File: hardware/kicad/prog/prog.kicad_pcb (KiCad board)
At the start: 4 copper layers, 174 x 134 mm, 123 parts, among them J1 AES_PROG, J2 Câble PROG-CHA, J3 CONF P, J4 CONF V, U1 AMS1117-3.3, U10 iCE40HX4K-TQ144, U11 W9825G6KH-6, U12 iCE40HX4K-TQ144, U13 W9825G6KH-6, U2 AP2112K-1.2, U3 74LVC16244A, U4 74LVC16244A, U5 74LVC16244A, U6 74LVC16245A, U7 74LVC16245A, U8 74AHCT125, U9 74LVC1G07, X1 25 MHz 3,3 V, X2 25 MHz 3,3 V

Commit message: PCB : vias vers les plans écartés de toutes les pastilles CMS
Freerouting refuse un via sur une pastille, même de son réseau.

Co-Authored-By: Claude Opus 5.5 <noreply@anthropic.com>
Claude-Session: https://claude.ai/code/session_01WKfXP1YJ8otGxZ5dsY6Agh
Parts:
- moved R6 39.1 mm to (128.6, 140.3)
- moved R4 34.7 mm to (131.1, 140.3)
- moved R5 28.2 mm to (128.6, 132.3)
- moved R3 25.7 mm to (128.6, 136.3)
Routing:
- net +3V3: track 137.5 -> 134.7 mm, vias 115 -> 114
- net GND: track 245.2 -> 246.8 mm

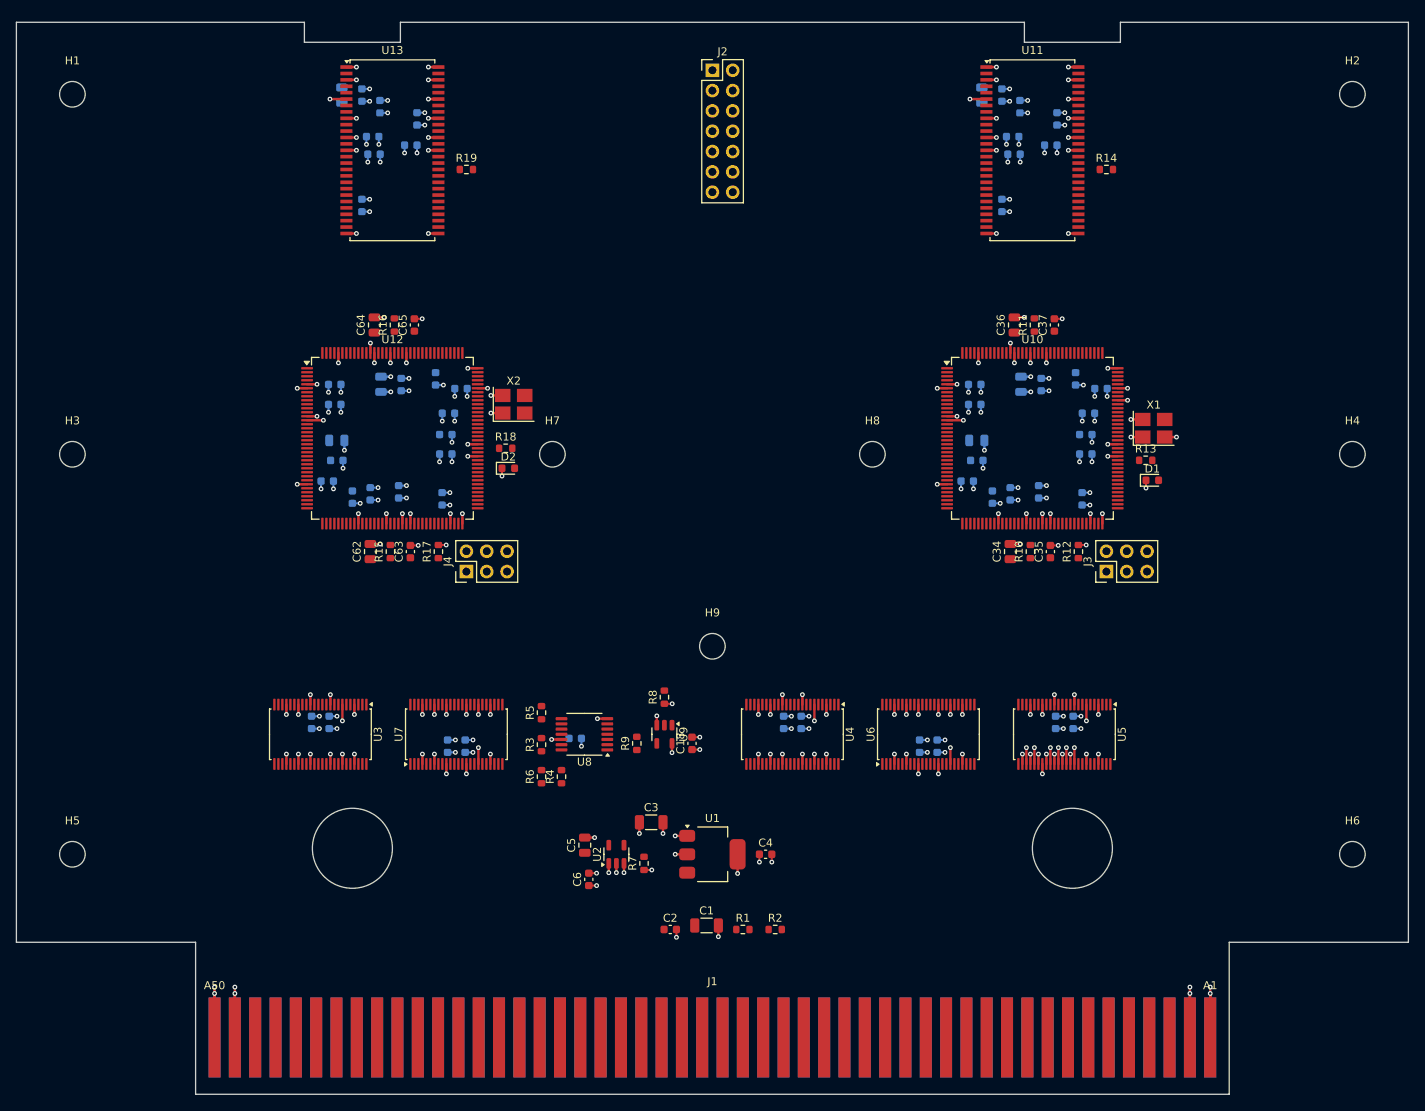
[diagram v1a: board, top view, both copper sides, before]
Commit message: Carte PROG routée (4 couches) : 3 raccordements aux plans restant à la main
Routage Freerouting en 12 passes, import, raccordements aux plans
complétés après routage (route.py --patch : via par pastille de masse
ou +3V3 restée seule, en évitant les pistes routées ; piste sur la face
de la pastille, ce qui corrige les contacts de masse côté B).
DRC KiCad : aucune violation d'isolement ni court-circuit ; 3 pastilles
à relier à la main (X2.2 GND, U12.100 +3V3, C46.1 +3V3) ; le reste =
sérigraphie et bibliothèque non déclarée dans l'environnement.
pcb.py : recherche de position des vias élargie (diagonales, 3 mm),
fonction plane_vias réutilisable.

Co-Authored-By: Claude Opus 5.5 <noreply@anthropic.com>
Claude-Session: https://claude.ai/code/session_01WKfXP1YJ8otGxZ5dsY6Agh
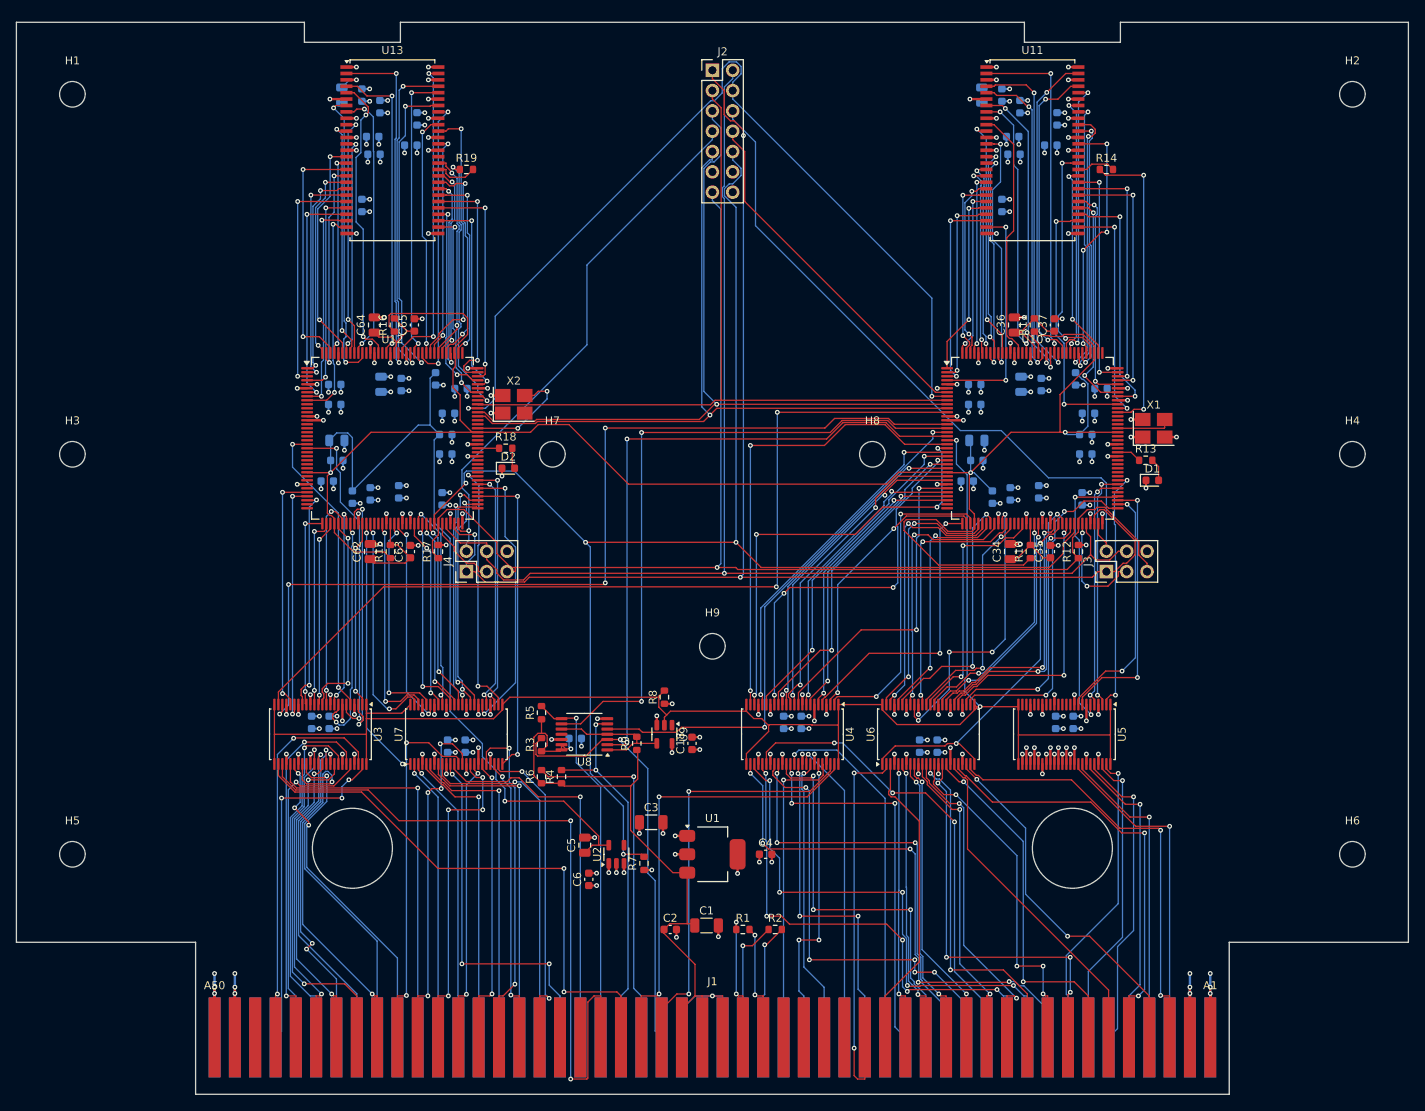
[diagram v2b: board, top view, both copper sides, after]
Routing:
- net +1V2: track 0.00 -> 334.1 mm, vias 0 -> 4
- net XLAT_EN_N: track 0.00 -> 199.8 mm, vias 0 -> 2
- net CDONE: track 0.00 -> 187.7 mm, vias 0 -> 4
- net PROG_SCK: track 0.00 -> 169.3 mm, vias 0 -> 3
- net PROG_IO0: track 0.00 -> 159.5 mm, vias 0 -> 1
- net CRESET_N: track 0.00 -> 159.3 mm, vias 0 -> 1
- net PORTWEL_N: track 0.00 -> 120.5 mm, vias 0 -> 4
- net PROG_IO2: track 0.00 -> 115.1 mm, vias 0 -> 2
- net PORTWEU_N: track 0.00 -> 112.4 mm, vias 0 -> 2
- net +5V: track 0.00 -> 109.1 mm, vias 0 -> 2
- net PROG_IO3: track 0.00 -> 99.0 mm, vias 0 -> 1
- net PROG_IO1: track 0.00 -> 98.1 mm
- net MODE: track 0.00 -> 94.0 mm, vias 0 -> 1
- net AES_PORTWEL: track 0.00 -> 91.0 mm, vias 0 -> 2
- net CS_P: track 0.00 -> 85.1 mm
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
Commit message: PCB : entretoises H7 et H8 remontées à y = 75 mm
En (130, 100) et (170, 100), elles bouchaient le couloir de sortie du
côté droit du FPGA V / SM (6 lignes du bus P et 2 raccordements non
routés sur la carte CHA). Cartes régénérées, contrôle Freerouting sans
violation ; nouveau routage en cours.

Co-Authored-By: Claude Opus 5.5 <noreply@anthropic.com>
Claude-Session: https://claude.ai/code/session_01WKfXP1YJ8otGxZ5dsY6Agh
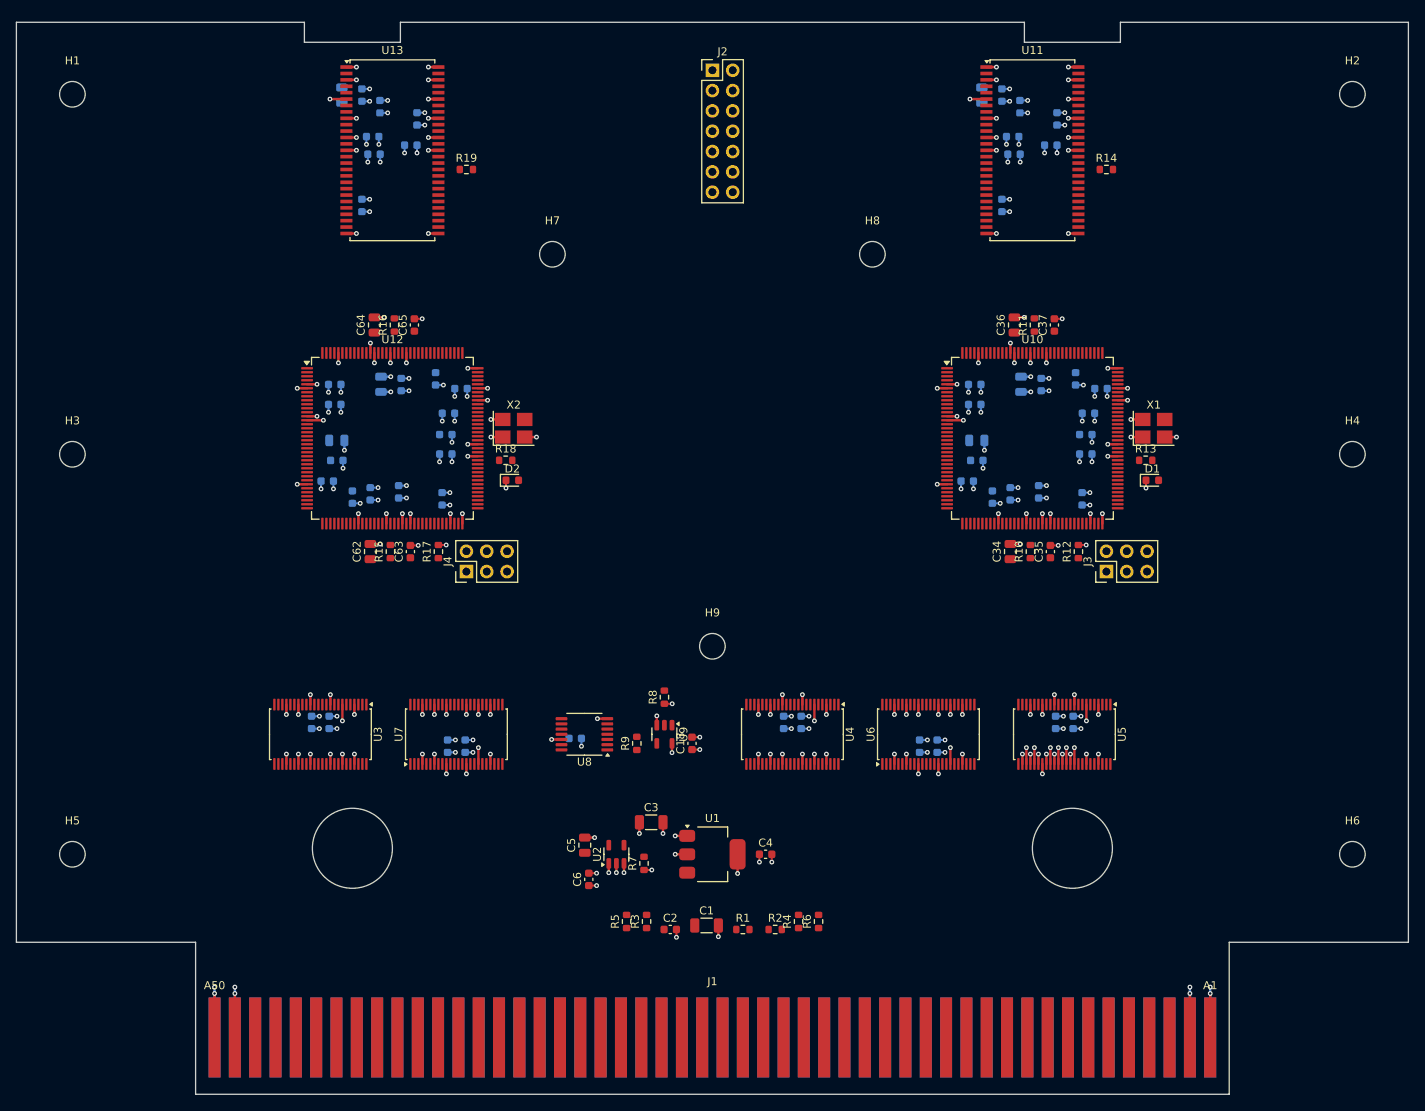
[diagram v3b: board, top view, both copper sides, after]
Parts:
- moved R6 39.1 mm to (163.3, 158.4)
- moved R4 34.7 mm to (160.8, 158.4)
- moved R5 28.2 mm to (139.3, 158.4)
- moved R3 25.7 mm to (141.8, 158.4)
- moved H7 25.0 mm to (130.0, 75.0)
- moved H8 25.0 mm to (170.0, 75.0)
- moved X2 3.00 mm to (125.2, 96.8)
- moved D2 1.58 mm to (125.0, 103.2)
- moved R18 1.50 mm to (124.2, 100.8)
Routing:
- net +1V2: track 334.1 -> 0.00 mm, vias 4 -> 0
- net XLAT_EN_N: track 199.8 -> 0.00 mm, vias 2 -> 0
- net CDONE: track 187.7 -> 0.00 mm, vias 4 -> 0
- net PROG_SCK: track 169.3 -> 0.00 mm, vias 3 -> 0
- net PROG_IO0: track 159.5 -> 0.00 mm, vias 1 -> 0
- net CRESET_N: track 159.3 -> 0.00 mm, vias 1 -> 0
- net PORTWEL_N: track 120.5 -> 0.00 mm, vias 4 -> 0
- net PROG_IO2: track 115.1 -> 0.00 mm, vias 2 -> 0
- net PORTWEU_N: track 112.4 -> 0.00 mm, vias 2 -> 0
- net +5V: track 109.1 -> 0.00 mm, vias 2 -> 0
- net PROG_IO3: track 99.0 -> 0.00 mm, vias 1 -> 0
- net PROG_IO1: track 98.1 -> 0.00 mm
- net MODE: track 94.0 -> 0.00 mm, vias 1 -> 0
- net AES_PORTWEL: track 91.0 -> 0.00 mm, vias 2 -> 0
- net CS_P: track 85.1 -> 0.00 mm
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
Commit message: Carte PROG routée : une seule pastille à relier à la main (C46.1)
Après le déplacement des entretoises H7/H8 : tous les signaux et
raccordements aux plans routés sauf le +3V3 de C46 (découplage de la
SDRAM P). DRC : aucune violation d'isolement ni court-circuit.

Co-Authored-By: Claude Opus 5.5 <noreply@anthropic.com>
Claude-Session: https://claude.ai/code/session_01WKfXP1YJ8otGxZ5dsY6Agh
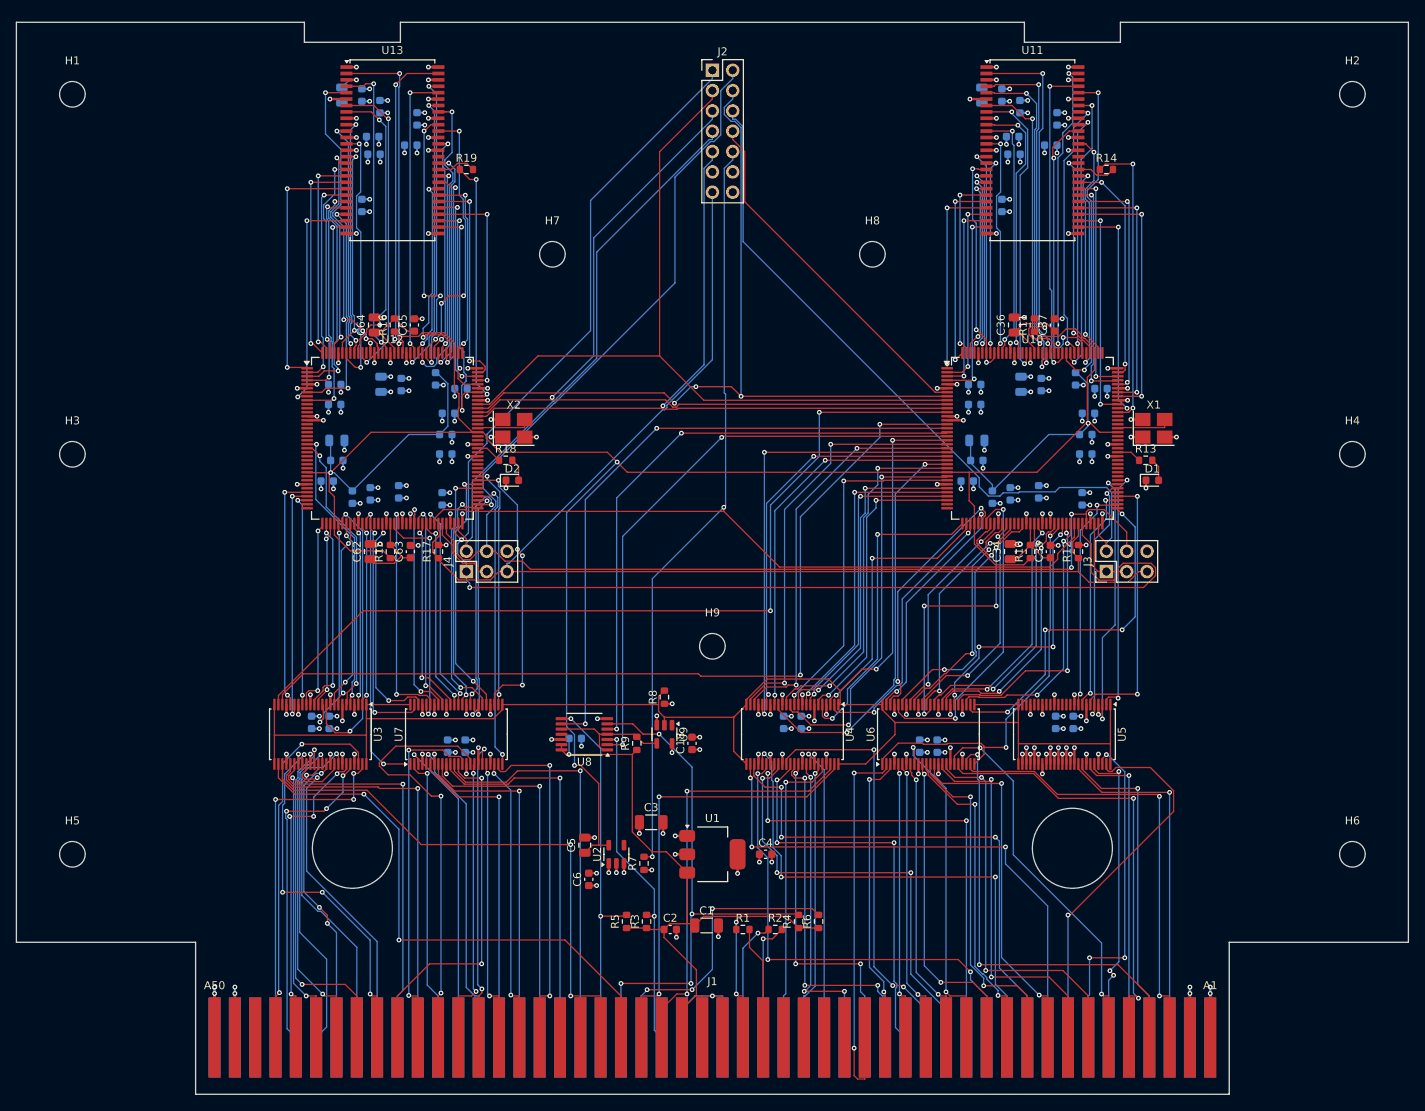
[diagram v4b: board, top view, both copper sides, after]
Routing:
- net +1V2: track 0.00 -> 299.3 mm, vias 0 -> 4
- net XLAT_EN_N: track 0.00 -> 215.3 mm, vias 0 -> 2
- net PROG_SCK: track 0.00 -> 182.2 mm, vias 0 -> 2
- net CDONE: track 0.00 -> 181.7 mm, vias 0 -> 2
- net PROG_IO0: track 0.00 -> 176.1 mm, vias 0 -> 2
- net CRESET_N: track 0.00 -> 161.4 mm
- net +5V: track 0.00 -> 112.5 mm, vias 0 -> 2
- net PORTWEL_N: track 0.00 -> 111.1 mm, vias 0 -> 2
- net PORTWEU_N: track 0.00 -> 110.3 mm, vias 0 -> 2
- net PROG_IO3: track 0.00 -> 104.3 mm, vias 0 -> 1
- net PROG_IO2: track 0.00 -> 101.1 mm, vias 0 -> 3
- net PROG_IO1: track 0.00 -> 99.4 mm
- net MODE: track 0.00 -> 93.8 mm, vias 0 -> 1
- net CS_P: track 0.00 -> 89.2 mm
- net PWAIT1_N: track 0.00 -> 79.9 mm, vias 0 -> 2
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
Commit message: PCB : carte PROG entièrement routée ; CHA à 2 liaisons (DOTA, GAD0)
Routeur de finition : PROG -> dernier raccordement (+3V3 de C46) fait,
plus aucune liaison manquante ; CHA -> P4 routé (et réseaux voisins
rerouttés), restent DOTA et GAD0 dont les broches d'entrée du tampon U7
sont enfermées par les pistes FIXD qui longent sa rangée. DRC des deux
cartes : aucune violation d'isolement ni court-circuit (restent
sérigraphie et bibliothèque non déclarée dans l'environnement).

Co-Authored-By: Claude Opus 5.5 <noreply@anthropic.com>
Claude-Session: https://claude.ai/code/session_01WKfXP1YJ8otGxZ5dsY6Agh
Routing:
- net +3V3: track 138.2 -> 138.7 mm, vias 115 -> 116
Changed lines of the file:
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@@
   (via locked (at 117.795388 92.762487) (size 0.6) (drill 0.3) (layers "F.Cu" "B.Cu") (net 2))
   (via locked (at 193.875 132.739999) (size 0.6) (drill 0.3) (layers "F.Cu" "B.Cu") (net 2))
+  (via (at 184.1854 53.3) (size 0.6) (drill 0.3) (layers "F.Cu" "B.Cu") (net 2))
   (via locked (at 98.25 137.475) (size 0.6) (drill 0.3) (layers "F.Cu" "B.Cu") (net 2))
   (via locked (at 109.412972 55.773548) (size 0.6) (drill 0.3) (layers "F.Cu" "B.Cu") (net 2))
@@
   (via locked (at 201.9 93.25) (size 0.6) (drill 0.3) (layers "F.Cu" "B.Cu") (net 2))
   (segment locked (start 161.1 132.739999) (end 162.075 132.739999) (width 0.25) (layer "B.Cu") (net 2))
+  (segment (start 183.9854 53.5) (end 183.9854 53.6) (width 0.127) (layer "B.Cu") (net 2))
   (segment locked (start 178.1 135.71) (end 179.075 135.71) (width 0.25) (layer "B.Cu") (net 2))
   (segment (start 113.077 57.3005) (end 113.0767 57.3005) (width 0.127) (layer "B.Cu") (net 2))
@@
   (segment locked (start 196.233668 94.877732) (end 196.233668 95.852731) (width 0.25) (layer "B.Cu") (net 2))
   (segment locked (start 117.795388 91.787488) (end 117.795388 92.762487) (width 0.25) (layer "B.Cu") (net 2))
+  (segment (start 184.1854 53.3) (end 183.9854 53.5) (width 0.127) (layer "B.Cu") (net 2))
   (segment locked (start 115.897358 99.969333) (end 115.897358 100.944333) (width 0.25) (layer "B.Cu") (net 2))
   (segment locked (start 158.9 132.739999) (end 159.875 132.739999) (width 0.25) (layer "B.Cu") (net 2))
@@
   (segment (start 196.2129 104.795) (end 196.2125 104.7954) (width 0.127) (layer "B.Cu") (net 2))
   (segment locked (start 191.102161 90.509689) (end 192.077161 90.509689) (width 0.25) (layer "B.Cu") (net 2))
+  (segment (start 183.9854 53.6) (end 183.8854 53.7) (width 0.127) (layer "B.Cu") (net 2))
   (segment locked (start 187.231055 104.171793) (end 188.206055 104.171793) (width 0.25) (layer "B.Cu") (net 2))
   (segment locked (start 108.437972 55.773548) (end 109.412972 55.773548) (width 0.25) (layer "B.Cu") (net 2))
